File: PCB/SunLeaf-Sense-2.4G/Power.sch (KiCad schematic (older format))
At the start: 18 parts

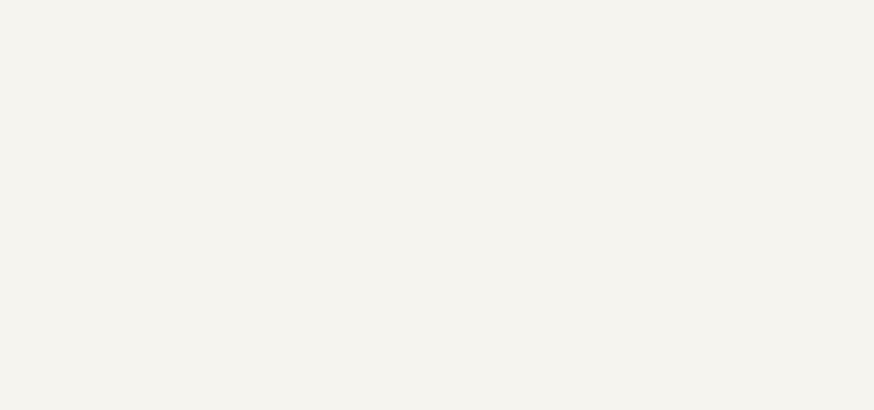
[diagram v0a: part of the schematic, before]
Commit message: Sensors Added
Sensors added to schematic page, project setup around new 2G module from ST
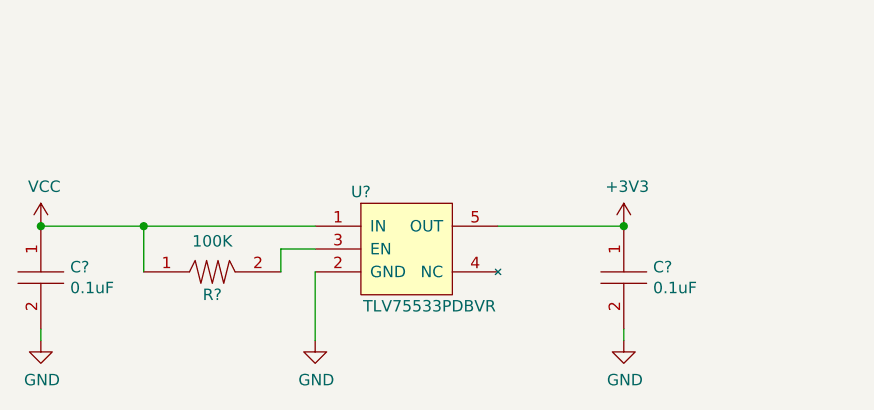
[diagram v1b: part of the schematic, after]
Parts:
- added C? (x2): C0402C104K9PACTU, AVR-KiCAD-Lib-Resistors:R0402, symbol AVR-KiCAD-Lib-Capacitors:C0402C104K9PACTU
- added R?: RC0603FR-07100KL, AVR-KiCAD-Lib-Resistors:R0603, symbol AVR-KiCAD-Lib-Resistors:RC0603FR-07100KL
- added U?: TLV75533PDBVR, AVR-KiCAD-Lib-ICs:TLV75533PDBVR, symbol AVR-KiCAD-Lib-ICs:TLV75533PDBVR
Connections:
- net +3V3: now also C?.1, U?.5 (OUT)
- net GND: now also C?.2, C?.2, U?.2 (GND)
- new net: R?.2, U?.3 (EN)
- new net VCC: C?.1, R?.1, U?.1 (IN)
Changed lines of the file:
@@
 $Descr A4 11693 8268
 encoding utf-8
-Sheet 4 5
+Sheet 2 4
 Title ""
 Date ""
@@
 Wire Wire Line
 	8700 3200 9000 3200
+Wire Wire Line
+	3750 7100 3750 7050
+$Comp
+L power:GND #PWR?
+U 1 1 603CEE82
+P 3750 7100
+F 0 "#PWR?" H 3750 6850 50  0001 C CNN
+F 1 "GND" H 3755 6927 50  0000 C CNN
+F 2 "" H 3750 7100 50  0001 C CNN
+F 3 "" H 3750 7100 50  0001 C CNN
+	1    3750 7100
+	1    0    0    -1
+$EndComp
+Connection ~ 3750 6600
+$Comp
+L AVR-KiCAD-Lib-Capacitors:C0402C104K9PACTU C?
+U 1 1 603CEEA2
+P 3750 6800
+F 0 "C?" V 3729 6928 50  0000 L CNN
+F 1 "C0402C104K9PACTU" H 3800 7000 50  0001 C CNN
+F 2 "AVR-KiCAD-Lib-Resistors:R0402" H 3550 6800 50  0001 C CNN
+F 3 "https://content.kemet.com/datasheets/KEM_C1006_X5R_SMD.pdf" H 3650 6900 50  0001 C CNN
+F 4 "0.10000" H 3850 7050 50  0001 C CNN "Cost QTY: 1"
+F 5 "0.01139" H 3950 7150 50  0001 C CNN "Cost QTY: 1000"
+F 6 "0.01035" H 4050 7250 50  0001 C CNN "Cost QTY: 2500"
+F 7 "0.00952" H 4150 7350 50  0001 C CNN "Cost QTY: 5000"
+F 8 "0.00756" H 4250 7450 50  0001 C CNN "Cost QTY: 10000"
+F 9 "KEMET" H 4350 7550 50  0001 C CNN "MFR"
+F 10 "C0402C104K9PACTU" H 4450 7650 50  0001 C CNN "MFR#"
+F 11 "Digikey" H 4550 7750 50  0001 C CNN "Vendor"
+F 12 "399-3026-6-ND" H 4650 7850 50  0001 C CNN "Vendor #"
+F 13 "AVR" H 4750 7950 50  0001 C CNN "Designer"
+F 14 "0.55mm" H 4850 8050 50  0001 C CNN "Height"
+F 15 "12/7/2019" H 5950 9150 50  0001 C CNN "Date Created"
+F 16 "12/7/2019" H 4950 8150 50  0001 C CNN "Date Modified"
+F 17 "Yes" H 5050 8250 50  0001 C CNN "Lead-Free ?"
+F 18 "1" H 5150 8350 50  0001 C CNN "RoHS Levels"
+F 19 "SMT" H 5250 8450 50  0001 C CNN "Mounting"
+F 20 "2" H 5350 8550 50  0001 C CNN "Pin Count #"
+F 21 "Active" H 5450 8650 50  0001 C CNN "Status"
+F 22 "10%" H 5550 8750 50  0001 C CNN "Tolerance"
+F 23 "Ceramic Cap" H 5650 8850 50  0001 C CNN "Type"
+F 24 "6.3V" H 5750 8950 50  0001 C CNN "Voltage"
+F 25 "0402" H 5850 9100 50  0001 C CNN "Package"
+F 26 "0.1µF ±10% 6.3V Ceramic Capacitor X5R 0402 (1005 Metric)" H 6250 9500 50  0001 C CNN "Description"
+F 27 "0.1uF" V 3820 6928 50  0000 L CNN "_Value_"
+F 28 "*" H 6150 9400 50  0001 C CNN "Management_ID"
+	1    3750 6800
+	0    1    1    0
+$EndComp
+$Comp
+L power:+3V3 #PWR?
+U 1 1 603CEEA8
+P 3750 6600
+F 0 "#PWR?" H 3750 6450 50  0001 C CNN
+F 1 "+3V3" H 3765 6773 50  0000 C CNN
+F 2 "" H 3750 6600 50  0001 C CNN
+F 3 "" H 3750 6600 50  0001 C CNN
+	1    3750 6600
+	1    0    0    -1
+$EndComp
+$Comp
+L power:GND #PWR?
+U 1 1 603CEEAE
+P 2400 7100
+F 0 "#PWR?" H 2400 6850 50  0001 C CNN
+F 1 "GND" H 2405 6927 50  0000 C CNN
+F 2 "" H 2400 7100 50  0001 C CNN
+F 3 "" H 2400 7100 50  0001 C CNN
+	1    2400 7100
+	1    0    0    -1
+$EndComp
+$Comp
+L AVR-KiCAD-Lib-ICs:TLV75533PDBVR U?
+U 1 1 603CEECD
+P 2600 6300
+F 0 "U?" H 2600 6150 50  0000 C CNN
+F 1 "TLV75533PDBVR" H 2650 6400 50  0001 C CNN
+F 2 "AVR-KiCAD-Lib-ICs:TLV75533PDBVR" H 2400 6200 50  0001 C CNN
+F 3 "https://www.ti.com/lit/ds/symlink/tlv755p.pdf?HQS=dis-dk-null-digikeymode-dsf-pf-null-wwe&ts=1613655963783" H 2500 6300 50  0001 C CNN
+F 4 "0.42000" H 2700 6550 50  0001 C CNN "Cost QTY: 1"
+F 5 "0.14787" H 2800 6650 50  0001 C CNN "Cost QTY: 1000"
+F 6 "*" H 2900 6750 50  0001 C CNN "Cost QTY: 2500"
+F 7 "*" H 3000 6850 50  0001 C CNN "Cost QTY: 5000"
+F 8 "*" H 3100 6950 50  0001 C CNN "Cost QTY: 10000"
+F 9 "Texas Instruments" H 3200 7050 50  0001 C CNN "MFR"
+F 10 "TLV75533PDBVR" H 3300 7150 50  0001 C CNN "MFR#"
+F 11 "Digikey" H 3400 7250 50  0001 C CNN "Vendor"
+F 12 "296-50411-2-ND" H 3500 7350 50  0001 C CNN "Vendor #"
+F 13 "AVR" H 3600 7450 50  0001 C CNN "Designer"
+F 14 "*" H 3700 7550 50  0001 C CNN "Height"
+F 15 "2/18/2021" H 4800 8650 50  0001 C CNN "Date Created"
+F 16 "2/18/2021" H 3800 7650 50  0001 C CNN "Date Modified"
+F 17 "Yes" H 3900 7750 50  0001 C CNN "Lead-Free ?"
+F 18 "1" H 4000 7850 50  0001 C CNN "RoHS Levels"
+F 19 "SMT" H 4100 7950 50  0001 C CNN "Mounting"
+F 20 "5" H 4200 8050 50  0001 C CNN "Pin Count #"
+F 21 "Active" H 4300 8150 50  0001 C CNN "Status"
+F 22 "*" H 4400 8250 50  0001 C CNN "Tolerance"
+F 23 "LDO" H 4500 8350 50  0001 C CNN "Type"
+F 24 "3.3V 500MA" H 4600 8450 50  0001 C CNN "Voltage"
+F 25 "*" H 4700 8600 50  0001 C CNN "Package"
+F 26 "Linear Voltage Regulator IC Positive Fixed 1 Output  500mA SOT-23-5" H 5000 8900 50  0001 C CNN "Description"
+F 27 "TLV75533PDBVR" H 2900 5650 50  0000 C CNN "_Value_"
+F 28 "*" H 5000 8900 50  0001 C CNN "Management_ID"
+	1    2600 6300
+	1    0    0    -1
+$EndComp
+Wire Wire Line
+	2400 6800 2400 7100
+Wire Wire Line
+	3200 6600 3750 6600
+$Comp
+L AVR-KiCAD-Lib-Capacitors:C0402C104K9PACTU C?
+U 1 1 603CEEEE
+P 1200 6800
+F 0 "C?" V 1179 6928 50  0000 L CNN
+F 1 "C0402C104K9PACTU" H 1250 7000 50  0001 C CNN
+F 2 "AVR-KiCAD-Lib-Resistors:R0402" H 1000 6800 50  0001 C CNN
+F 3 "https://content.kemet.com/datasheets/KEM_C1006_X5R_SMD.pdf" H 1100 6900 50  0001 C CNN
+F 4 "0.10000" H 1300 7050 50  0001 C CNN "Cost QTY: 1"
+F 5 "0.01139" H 1400 7150 50  0001 C CNN "Cost QTY: 1000"
+F 6 "0.01035" H 1500 7250 50  0001 C CNN "Cost QTY: 2500"
+F 7 "0.00952" H 1600 7350 50  0001 C CNN "Cost QTY: 5000"
+F 8 "0.00756" H 1700 7450 50  0001 C CNN "Cost QTY: 10000"
+F 9 "KEMET" H 1800 7550 50  0001 C CNN "MFR"
+F 10 "C0402C104K9PACTU" H 1900 7650 50  0001 C CNN "MFR#"
+F 11 "Digikey" H 2000 7750 50  0001 C CNN "Vendor"
+F 12 "399-3026-6-ND" H 2100 7850 50  0001 C CNN "Vendor #"
+F 13 "AVR" H 2200 7950 50  0001 C CNN "Designer"
+F 14 "0.55mm" H 2300 8050 50  0001 C CNN "Height"
+F 15 "12/7/2019" H 3400 9150 50  0001 C CNN "Date Created"
+F 16 "12/7/2019" H 2400 8150 50  0001 C CNN "Date Modified"
+F 17 "Yes" H 2500 8250 50  0001 C CNN "Lead-Free ?"
+F 18 "1" H 2600 8350 50  0001 C CNN "RoHS Levels"
+F 19 "SMT" H 2700 8450 50  0001 C CNN "Mounting"
+F 20 "2" H 2800 8550 50  0001 C CNN "Pin Count #"
+F 21 "Active" H 2900 8650 50  0001 C CNN "Status"
+F 22 "10%" H 3000 8750 50  0001 C CNN "Tolerance"
+F 23 "Ceramic Cap" H 3100 8850 50  0001 C CNN "Type"
+F 24 "6.3V" H 3200 8950 50  0001 C CNN "Voltage"
+F 25 "0402" H 3300 9100 50  0001 C CNN "Package"
+F 26 "0.1µF ±10% 6.3V Ceramic Capacitor X5R 0402 (1005 Metric)" H 3700 9500 50  0001 C CNN "Description"
+F 27 "0.1uF" V 1270 6928 50  0000 L CNN "_Value_"
+F 28 "*" H 3600 9400 50  0001 C CNN "Management_ID"
+	1    1200 6800
+	0    1    1    0
+$EndComp
+Wire Wire Line
+	1200 7100 1200 7050
+$Comp
+L power:GND #PWR?
+U 1 1 603CEEF5
+P 1200 7100
+F 0 "#PWR?" H 1200 6850 50  0001 C CNN
+F 1 "GND" H 1205 6927 50  0000 C CNN
+F 2 "" H 1200 7100 50  0001 C CNN
+F 3 "" H 1200 7100 50  0001 C CNN
+	1    1200 7100
+	1    0    0    -1
+$EndComp
+Wire Wire Line
+	2400 6700 2250 6700
+$Comp
+L AVR-KiCAD-Lib-Resistors:RC0603FR-07100KL R?
+U 1 1 603CEF15
+P 1950 6800
+F 0 "R?" H 1950 6700 50  0000 C CNN
+F 1 "RC0603FR-07100KL" H 1950 6934 50  0001 C CNN
+F 2 "AVR-KiCAD-Lib-Resistors:R0603" H 4250 9500 50  0001 C CNN
+F 3 "" H 1950 6800 50  0001 C CNN
+F 4 "0.10" H 2050 7050 50  0001 C CNN "Cost QTY: 1"
+F 5 "0.00476" H 2150 7150 50  0001 C CNN "Cost QTY: 1000"
+F 6 "0.00418" H 2250 7250 50  0001 C CNN "Cost QTY: 2500"
+F 7 "*" H 2350 7350 50  0001 C CNN "Cost QTY: 5000"
+F 8 "*" H 2450 7450 50  0001 C CNN "Cost QTY: 10000"
+F 9 "Yageo" H 2550 7550 50  0001 C CNN "MFR"
+F 10 "RC0603FR-07100KL" H 2650 7650 50  0001 C CNN "MFR#"
+F 11 "Digikey" H 2750 7750 50  0001 C CNN "Vendor"
+F 12 "311-100KHRCT-ND" H 2850 7850 50  0001 C CNN "Vendor #"
+F 13 "AVR" H 2950 7950 50  0001 C CNN "Designer"
+F 14 "0.55mm" H 3050 8050 50  0001 C CNN "Height"
+F 15 "4/23/2019" H 4150 9150 50  0001 C CNN "Date Created"
+F 16 "4/23/2019" H 3150 8150 50  0001 C CNN "Date Modified"
+F 17 "Yes" H 3250 8250 50  0001 C CNN "Lead-Free ?"
+F 18 "1" H 3350 8350 50  0001 C CNN "RoHS Levels"
+F 19 "SMT" H 3450 8450 50  0001 C CNN "Mounting"
+F 20 "2" H 3550 8550 50  0001 C CNN "Pin Count #"
+F 21 "Active" H 3650 8650 50  0001 C CNN "Status"
+F 22 "1%" H 3750 8750 50  0001 C CNN "Tolerance"
+F 23 "SMT Chip Resistor" H 3850 8850 50  0001 C CNN "Type"
+F 24 "*" H 3950 8950 50  0001 C CNN "Voltage"
+F 25 "0603" H 4050 9100 50  0001 C CNN "Package"
+F 26 "100K" H 1950 6934 50  0000 C CNN "_Value_"
+F 27 "*" H 4350 9400 50  0001 C CNN "Management_ID"
+F 28 "RES SMD 100K OHM 1% 1/10W 0603" H 4350 9400 50  0001 C CNN "Description"
+	1    1950 6800
+	1    0    0    -1
+$EndComp
+$Comp
+L power:VCC #PWR?
+U 1 1 603CEF1B
+P 1200 6600
+F 0 "#PWR?" H 1200 6450 50  0001 C CNN
+F 1 "VCC" H 1215 6773 50  0000 C CNN
+F 2 "" H 1200 6600 50  0001 C CNN
+F 3 "" H 1200 6600 50  0001 C CNN
+	1    1200 6600
+	1    0    0    -1
+$EndComp
+Connection ~ 1200 6600
+Wire Wire Line
+	1200 6600 1650 6600
+Wire Wire Line
+	2250 6700 2250 6800
+Wire Wire Line
+	1650 6800 1650 6600
+Connection ~ 1650 6600
+Wire Wire Line
+	1650 6600 2400 6600
 $EndSCHEMATC

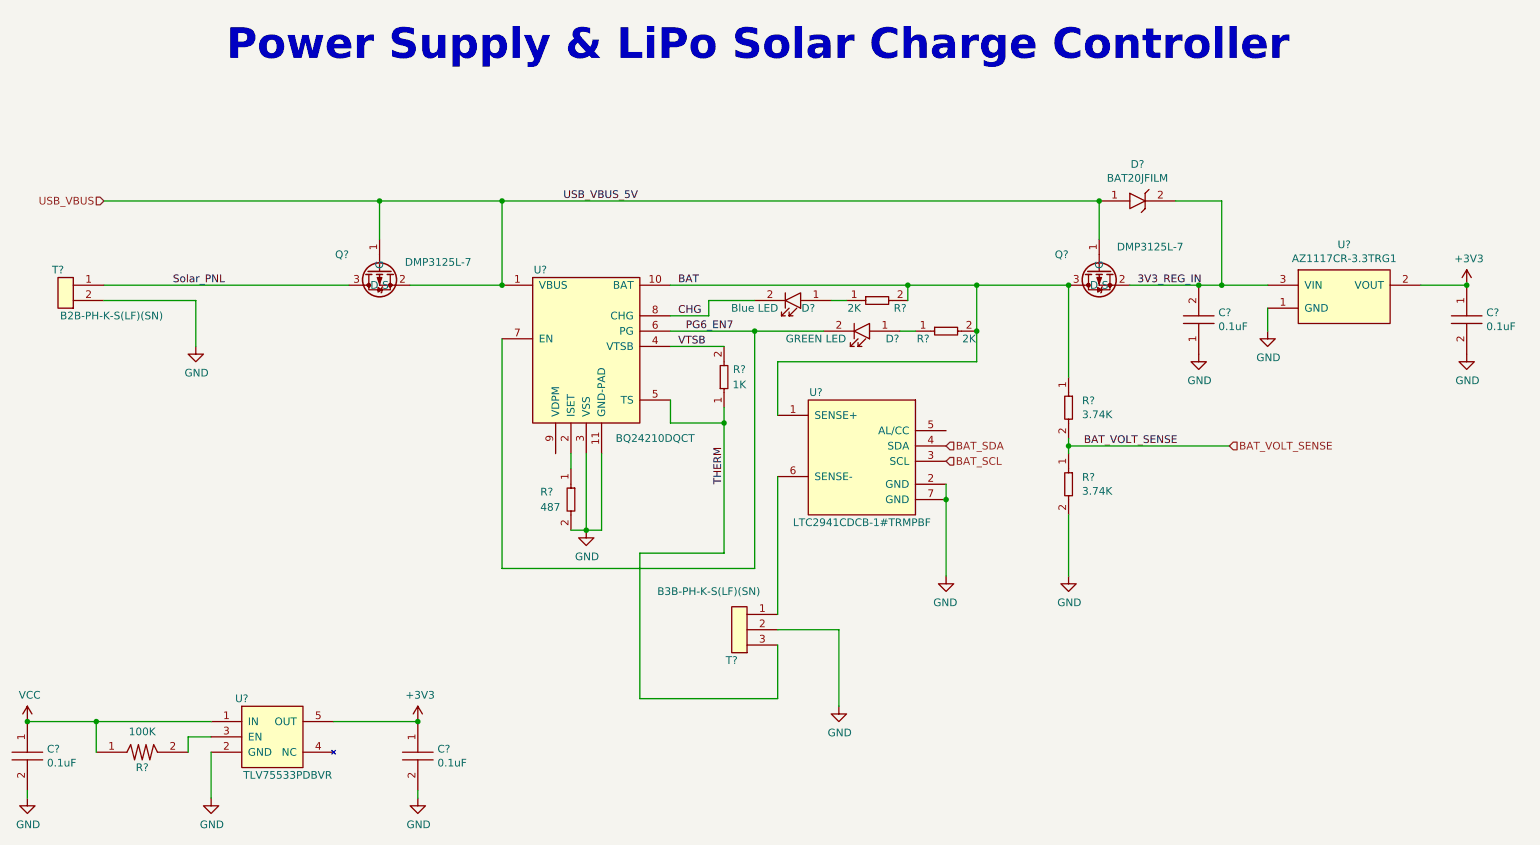
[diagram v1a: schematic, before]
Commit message: PCB
PCB started, PAR sensor circuitry integrated into design
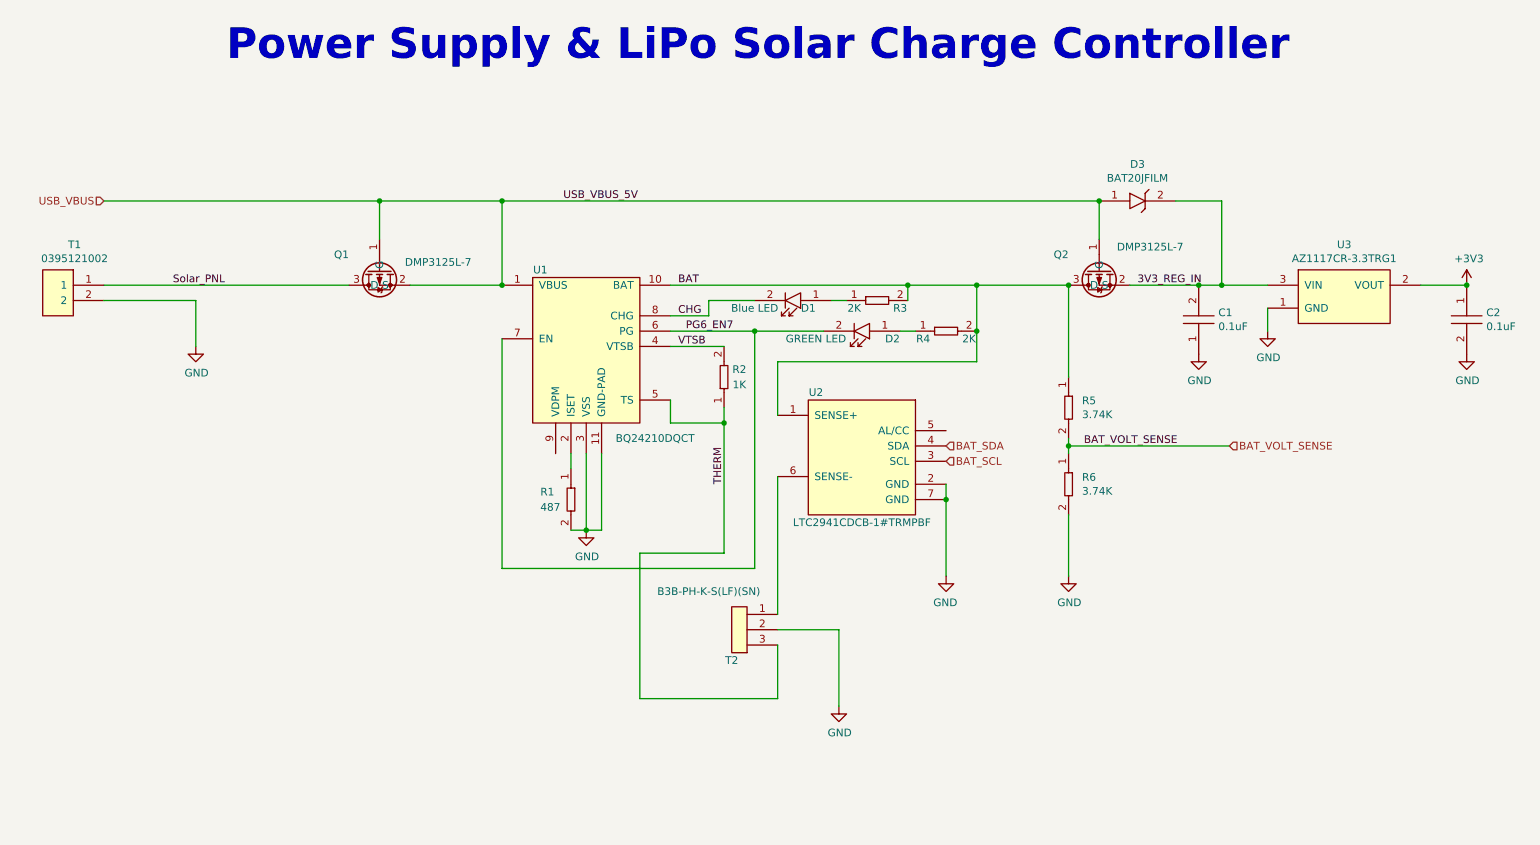
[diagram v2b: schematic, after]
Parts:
- removed C? (x2): C0402C104K9PACTU, AVR-KiCAD-Lib-Resistors:R0402, symbol AVR-KiCAD-Lib-Capacitors:C0402C104K9PACTU
- removed R?: RC0603FR-07100KL, AVR-KiCAD-Lib-Resistors:R0603, symbol AVR-KiCAD-Lib-Resistors:RC0603FR-07100KL
- removed T?: B2B-PH-K-S(LF)(SN), AVR-KiCAD-Lib-Connectors:B2B-PH-K-S(LF)(SN), symbol AVR-KiCAD-Lib-Connectors:B2B-PH-K-S(LF)(SN)
- removed U?: TLV75533PDBVR, AVR-KiCAD-Lib-ICs:TLV75533PDBVR, symbol AVR-KiCAD-Lib-ICs:TLV75533PDBVR
- added T1: 0395121002, AVR-KiCAD-Lib-Connectors:0395121002, symbol AVR-KiCAD-Lib-Connectors:0395121002
- gave numbers to parts that had none: 17
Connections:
- net GND: now also T1.2
- net Solar_PNL: now also T1.1
